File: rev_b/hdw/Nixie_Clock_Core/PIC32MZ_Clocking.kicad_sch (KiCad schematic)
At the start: 17 parts, among them U1101 74LVC1G97, X1101 ASE-8.000MHz, X1102 ECS-327KE

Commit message: lots of rev B control board schematic progress
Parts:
- renumbered C1103 to C?, C1105 to C?, C1101 to C?, C1104 to C?, C1102 to C?, L1102 to L?, L1101 to L?, R1101 to R?, R1105 to R?, R1103 to R?, R1102 to R?, R1104 to R?, R1106 to R?, TP1101 to TP?, U1101 to U?, X1101 to X?, X1102 to X?

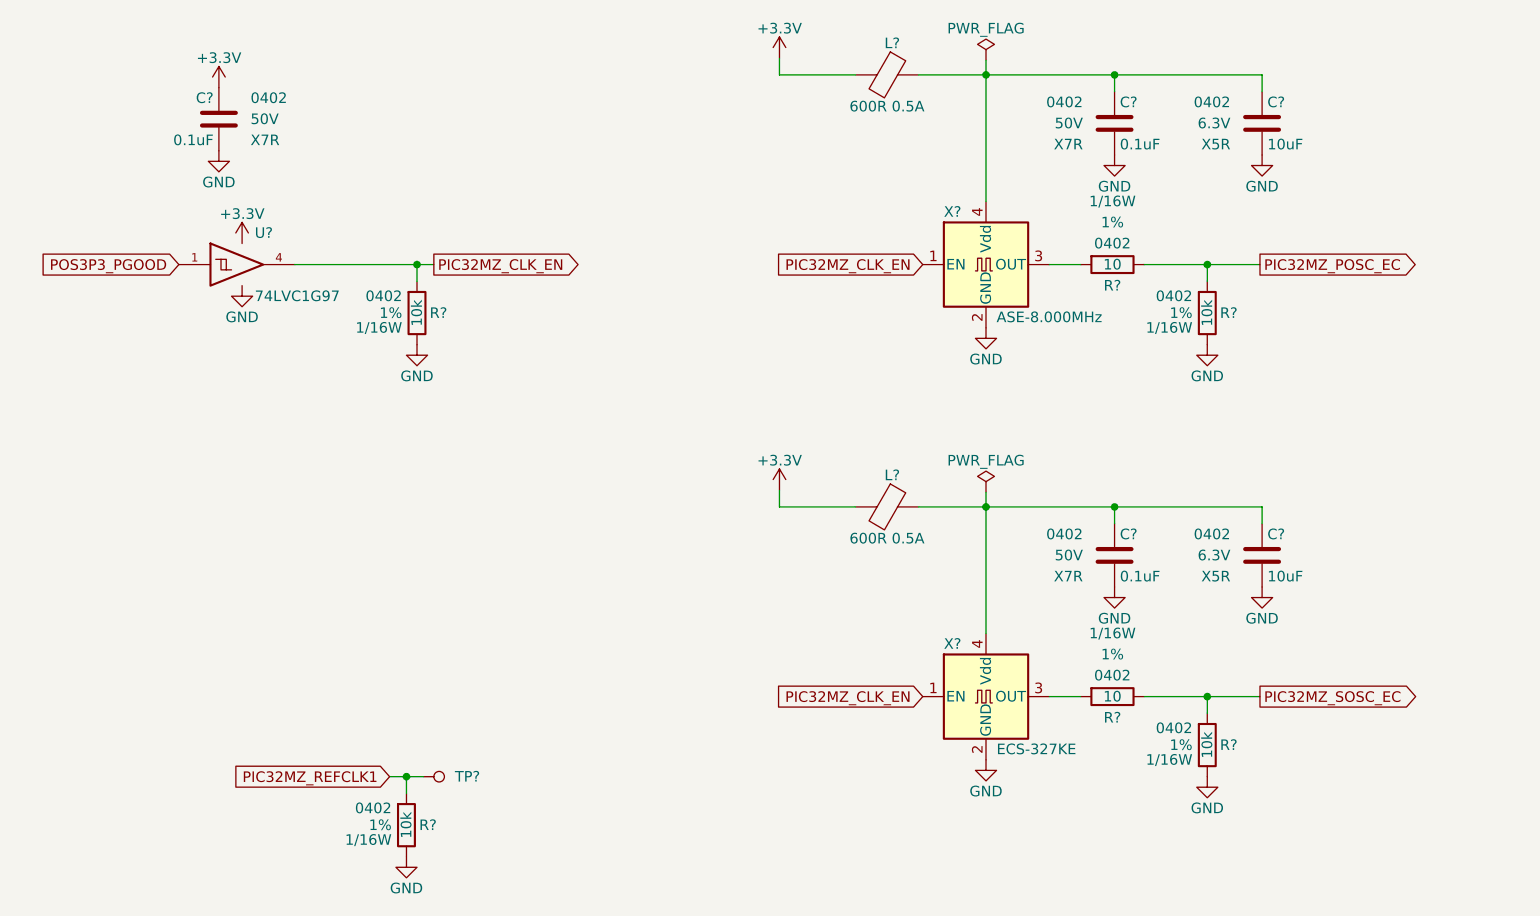
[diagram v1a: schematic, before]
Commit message: updated footprints, ran some DRC
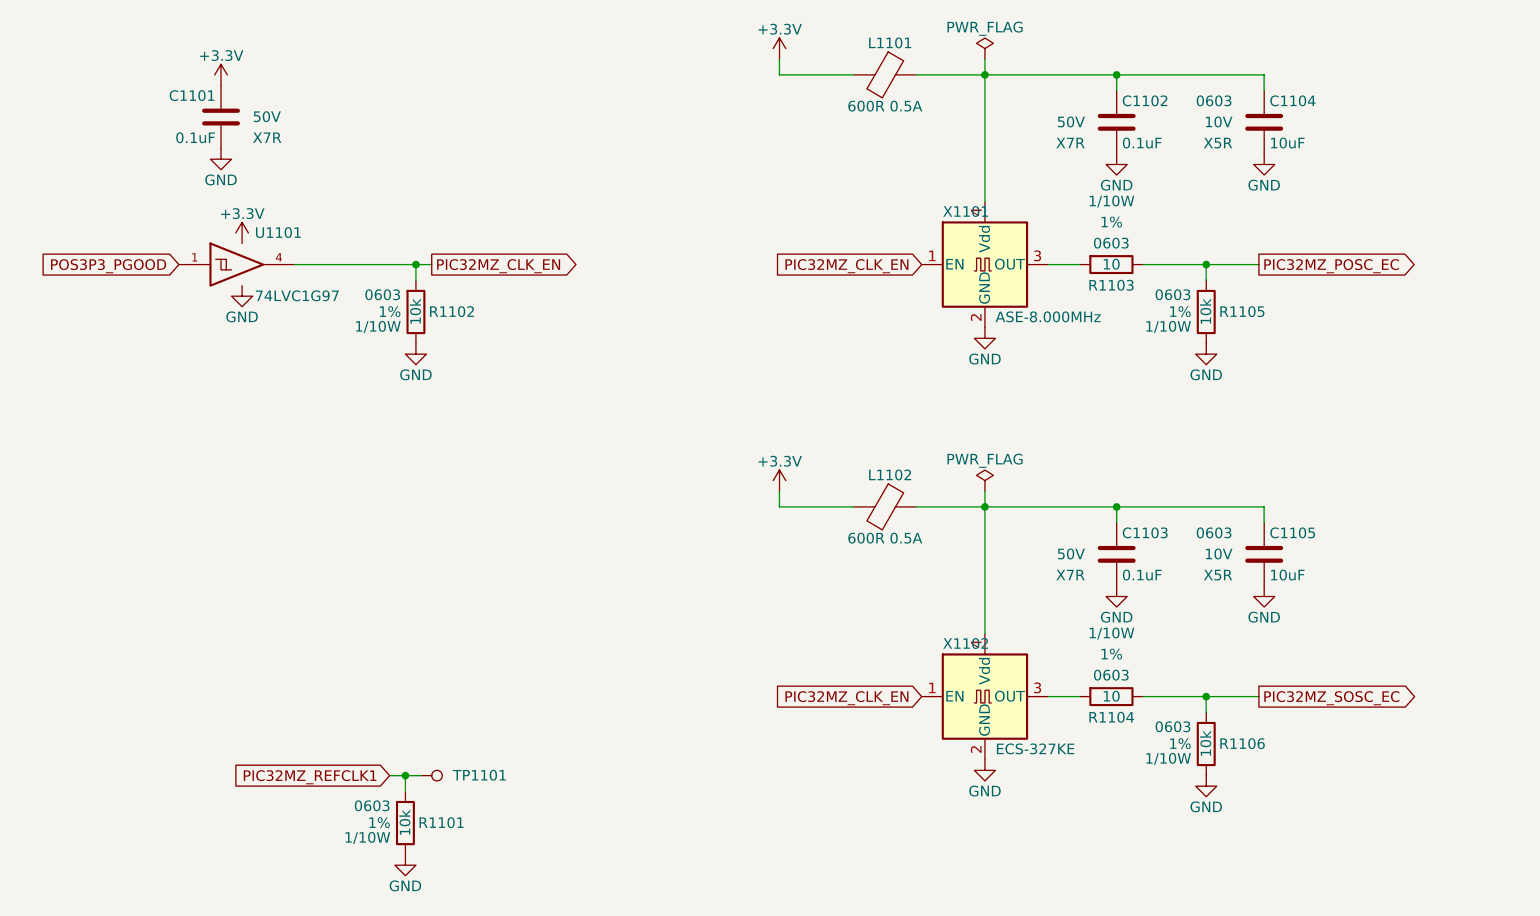
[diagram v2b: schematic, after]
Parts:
- C1101, C1102, C1103: renamed from C?; footprint Capacitors_SMD:C_0402 -> Capacitors_SMD:C_0603; Digi-Key PN 490-10698-1-ND -> (none); display_footprint 0402 -> (none)
- C1104, C1105: renamed from C?; footprint Capacitors_SMD:C_0402 -> Capacitors_SMD:C_0603; Digi-Key PN 1276-1451-1-ND -> (none); Voltage 6.3V -> 10V; display_footprint 0402 -> 0603
- L1101, L1102: renamed from L?; footprint Inductors_SMD:L_0402 -> Inductors_SMD:L_0603; Digi-Key PN 490-5441-1-ND -> (none)
- R1101, R1102, R1105, R1106: renamed from R?; footprint Resistors_SMD:R_0402 -> Resistors_SMD:R_0603; Digi-Key PN RMCF0402FT10K0CT-ND -> (none); Wattage 1/16W -> 1/10W; display_footprint 0402 -> 0603
- R1103, R1104: renamed from R?; footprint Resistors_SMD:R_0402 -> Resistors_SMD:R_0603; Digi-Key PN RMCF0402FT10R0CT-ND -> (none); Wattage 1/16W -> 1/10W; display_footprint 0402 -> 0603
- gave numbers to parts that had none: 4

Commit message: hid all passive refdes on core PCB
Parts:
- C1101, C1102, C1103: Digi-Key PN (none) -> 1276-1935-1-ND; display_footprint (none) -> 0603
- C1104, C1105: Digi-Key PN (none) -> 1276-1871-1-ND
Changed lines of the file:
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@@
       (effects (font (size 1.27 1.27)) hide)
     )
-    (property "display_footprint" "" (at 167.64 100.965 0)
+    (property "display_footprint" "0603" (at 167.64 100.965 0)
       (effects (font (size 1.27 1.27)) (justify right))
     )
@@
       (effects (font (size 1.27 1.27)) (justify right))
     )
-    (property "Digi-Key PN" "" (at 72.136 278.257 0)
+    (property "Digi-Key PN" "1276-1935-1-ND" (at 72.136 278.257 0)
       (effects (font (size 1.27 1.27)) hide)
     )
@@
       (effects (font (size 1.27 1.27)) (justify right))
     )
-    (property "Digi-Key PN" "" (at 189.23 103.505 0)
+    (property "Digi-Key PN" "1276-1871-1-ND" (at 189.23 103.505 0)
       (effects (font (size 1.27 1.27)) hide)
     )
@@
       (effects (font (size 1.27 1.27)) hide)
     )
-    (property "Digi-Key PN" "" (at 52.705 38.1 0)
+    (property "Digi-Key PN" "1276-1935-1-ND" (at 52.705 38.1 0)
       (effects (font (size 1.524 1.524)) hide)
     )
-    (property "display_footprint" "" (at 67.31 48.26 0)
+    (property "display_footprint" "0603" (at 67.31 48.26 0)
       (effects (font (size 1.27 1.27)) (justify right))
     )
@@
       (effects (font (size 1.27 1.27)) (justify right))
     )
-    (property "Digi-Key PN" "" (at 189.23 51.435 0)
+    (property "Digi-Key PN" "1276-1871-1-ND" (at 189.23 51.435 0)
       (effects (font (size 1.27 1.27)) hide)
     )
@@
       (effects (font (size 1.27 1.27)) hide)
     )
-    (property "display_footprint" "" (at 167.64 48.895 0)
+    (property "display_footprint" "0603" (at 167.64 48.895 0)
       (effects (font (size 1.27 1.27)) (justify right))
     )
@@
       (effects (font (size 1.27 1.27)) (justify right))
     )
-    (property "Digi-Key PN" "" (at 72.136 226.187 0)
-      (effects (font (size 1.27 1.27)) hide)
-    )
+    (property "Digi-Key PN" "1276-1935-1-ND" (at 72.136 226.187 0)
+      (effects (font (size 1.27 1.27)) hide)
+    )

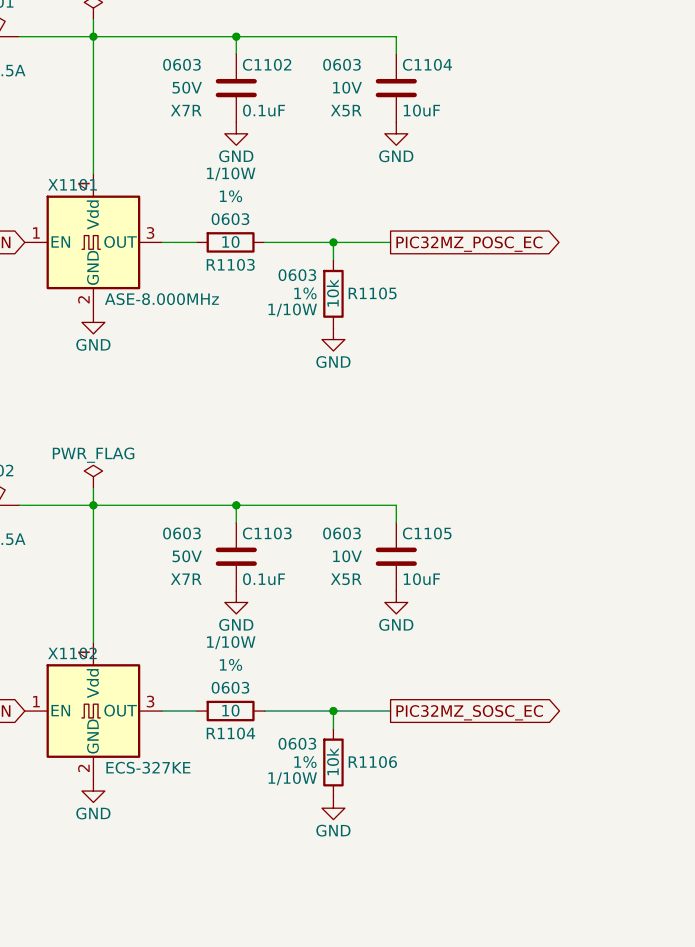
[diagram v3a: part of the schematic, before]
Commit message: started grouping MCU components on PCB
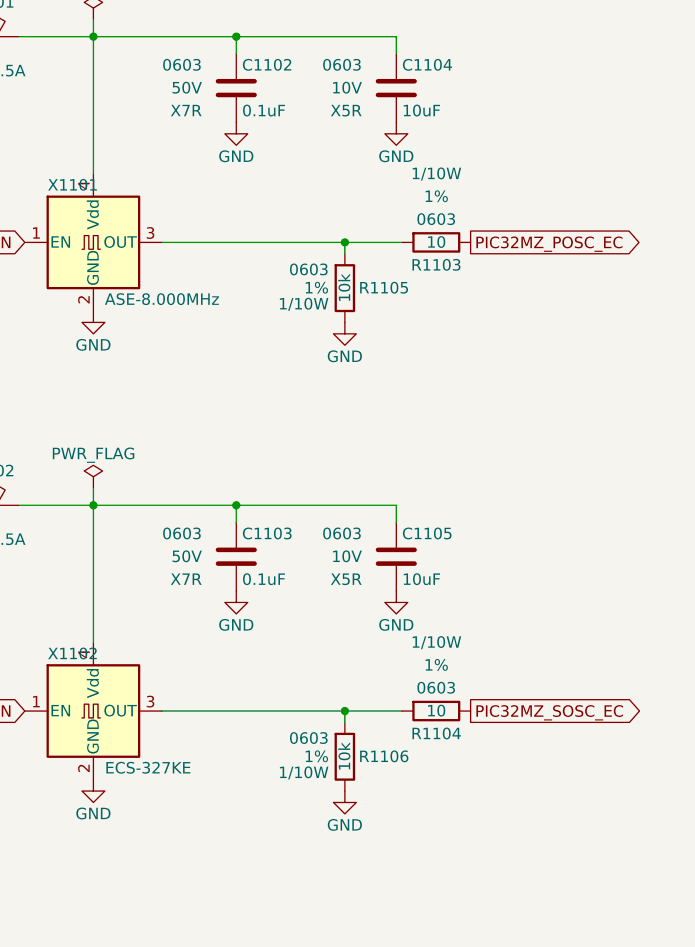
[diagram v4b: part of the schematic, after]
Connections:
- net PIC32MZ_POSC_EC: no longer R1105.1
- net PIC32MZ_SOSC_EC: no longer R1106.1
- net at R1103.1, X1101.3 (OUT): now also R1105.1
- net at R1104.1, X1102.3 (OUT): now also R1106.1
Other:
- moved on the sheet: R1103, R1104, R1105, R1106

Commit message: added BOM
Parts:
- L1101, L1102: Digi-Key PN (none) -> 490-1014-1-ND
- R1101, R1102, R1105, R1106: Digi-Key PN (none) -> 541-10.0KHCT-ND
- R1103, R1104: Digi-Key PN (none) -> 541-10.0HCT-ND
- U1101: Digi-Key PN 1727-1772-1-ND -> 296-15582-1-ND
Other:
- title: (none) -> Nixie Clock Redux Core Board
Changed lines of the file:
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@@
   (paper "A")
   (title_block
-    (date "2023-05-12")
-    (rev "PRELIM")
+    (title "Nixie Clock Redux Core Board")
+    (date "2023-07-30")
+    (rev "B")
     (company "Drew Maatman")
   )
@@
     (stroke (width 0) (type default))
   )
-  (global_label "PIC32MZ_CLK_EN" (shape input) (at 147.955 68.58 180)
+  (global_label "PIC32MZ_CLK_EN" (shape input) (at 147.955 68.58 180) (fields_autoplaced)
     (effects (font (size 1.27 1.27)) (justify right))
-    (property "Intersheetrefs" "${INTERSHEET_REFS}" (at 147.955 68.58 0)
-      (effects (font (size 1.27 1.27)) hide)
-    )
-  )
-  (global_label "PIC32MZ_REFCLK1" (shape input) (at 83.82 130.175 180)
+    (property "Intersheetrefs" "${INTERSHEET_REFS}" (at 128.8417 68.58 0)
+      (effects (font (size 1.27 1.27)) (justify right))
+    )
+  )
+  (global_label "PIC32MZ_REFCLK1" (shape input) (at 83.82 130.175 180) (fields_autoplaced)
     (effects (font (size 1.27 1.27)) (justify right))
-    (property "Intersheetrefs" "${INTERSHEET_REFS}" (at 83.82 130.175 0)
-      (effects (font (size 1.27 1.27)) hide)
-    )
-  )
-  (global_label "POS3P3_PGOOD" (shape input) (at 58.42 68.58 180)
+    (property "Intersheetrefs" "${INTERSHEET_REFS}" (at 63.4367 130.175 0)
+      (effects (font (size 1.27 1.27)) (justify right))
+    )
+  )
+  (global_label "POS3P3_PGOOD" (shape input) (at 58.42 68.58 180) (fields_autoplaced)
     (effects (font (size 1.27 1.27)) (justify right))
-    (property "Intersheetrefs" "${INTERSHEET_REFS}" (at 58.42 68.58 0)
-      (effects (font (size 1.27 1.27)) hide)
-    )
-  )
-  (global_label "PIC32MZ_SOSC_EC" (shape output) (at 197.485 120.65 0)
+    (property "Intersheetrefs" "${INTERSHEET_REFS}" (at 40.5766 68.58 0)
+      (effects (font (size 1.27 1.27)) (justify right))
+    )
+  )
+  (global_label "PIC32MZ_SOSC_EC" (shape output) (at 197.485 120.65 0) (fields_autoplaced)
     (effects (font (size 1.27 1.27)) (justify left))
-    (property "Intersheetrefs" "${INTERSHEET_REFS}" (at 197.485 120.65 0)
-      (effects (font (size 1.27 1.27)) hide)
-    )
-  )
-  (global_label "PIC32MZ_POSC_EC" (shape output) (at 197.485 68.58 0)
+    (property "Intersheetrefs" "${INTERSHEET_REFS}" (at 217.9892 120.65 0)
+      (effects (font (size 1.27 1.27)) (justify left))
+    )
+  )
+  (global_label "PIC32MZ_POSC_EC" (shape output) (at 197.485 68.58 0) (fields_autoplaced)
     (effects (font (size 1.27 1.27)) (justify left))
-    (property "Intersheetrefs" "${INTERSHEET_REFS}" (at 197.485 68.58 0)
-      (effects (font (size 1.27 1.27)) hide)
-    )
-  )
-  (global_label "PIC32MZ_CLK_EN" (shape output) (at 88.9 68.58 0)
+    (property "Intersheetrefs" "${INTERSHEET_REFS}" (at 218.0497 68.58 0)
+      (effects (font (size 1.27 1.27)) (justify left))
+    )
+  )
+  (global_label "PIC32MZ_CLK_EN" (shape output) (at 88.9 68.58 0) (fields_autoplaced)
     (effects (font (size 1.27 1.27)) (justify left))
-    (property "Intersheetrefs" "${INTERSHEET_REFS}" (at 88.9 68.58 0)
-      (effects (font (size 1.27 1.27)) hide)
-    )
-  )
-  (global_label "PIC32MZ_CLK_EN" (shape input) (at 147.955 120.65 180)
+    (property "Intersheetrefs" "${INTERSHEET_REFS}" (at 108.0133 68.58 0)
+      (effects (font (size 1.27 1.27)) (justify left))
+    )
+  )
+  (global_label "PIC32MZ_CLK_EN" (shape input) (at 147.955 120.65 180) (fields_autoplaced)
     (effects (font (size 1.27 1.27)) (justify right))
-    (property "Intersheetrefs" "${INTERSHEET_REFS}" (at 147.955 120.65 0)
-      (effects (font (size 1.27 1.27)) hide)
+    (property "Intersheetrefs" "${INTERSHEET_REFS}" (at 128.8417 120.65 0)
+      (effects (font (size 1.27 1.27)) (justify right))
     )
   )
@@
       (effects (font (size 1.27 1.27)) hide)
     )
-    (property "Digi-Key PN" "1727-1772-1-ND" (at 66.04 68.58 0)
+    (property "Digi-Key PN" "296-15582-1-ND" (at 66.04 68.58 0)
       (effects (font (size 1.27 1.27)) hide)
     )
@@
       (effects (font (size 1.27 1.27)) (justify left))
     )
-    (property "Digi-Key PN" "" (at 85.725 135.89 0)
+    (property "Digi-Key PN" "541-10.0KHCT-ND" (at 85.725 135.89 0)
       (effects (font (size 1.27 1.27)) hide)
     )
@@
       (effects (font (size 1.27 1.27)) hide)
     )
-    (property "Digi-Key PN" "" (at 65.024 -110.236 0)
+    (property "Digi-Key PN" "490-1014-1-ND" (at 65.024 -110.236 0)
       (effects (font (size 1.27 1.27)) hide)
     )
@@
       (effects (font (size 1.27 1.27)) hide)
     )
-    (property "Digi-Key PN" "" (at 65.024 -162.306 0)
+    (property "Digi-Key PN" "490-1014-1-ND" (at 65.024 -162.306 0)
       (effects (font (size 1.27 1.27)) hide)
     )
@@
       (effects (font (size 1.27 1.27)) (justify left))
     )
-    (property "Digi-Key PN" "" (at 183.515 73.66 0)
+    (property "Digi-Key PN" "541-10.0KHCT-ND" (at 183.515 73.66 0)
       (effects (font (size 1.27 1.27)) hide)
     )
@@
       (effects (font (size 1.27 1.27)))
     )
-    (property "Digi-Key PN" "" (at 183.515 60.96 0)
+    (property "Digi-Key PN" "541-10.0HCT-ND" (at 183.515 60.96 0)
       (effects (font (size 1.524 1.524)) hide)
     )
@@
       (effects (font (size 1.27 1.27)) (justify left))
     )
-    (property "Digi-Key PN" "" (at 86.995 74.295 0)
+    (property "Digi-Key PN" "541-10.0KHCT-ND" (at 86.995 74.295 0)
       (effects (font (size 1.27 1.27)) hide)
     )
@@
       (effects (font (size 1.27 1.27)))
     )
-    (property "Digi-Key PN" "" (at 183.515 113.03 0)
+    (property "Digi-Key PN" "541-10.0HCT-ND" (at 183.515 113.03 0)
       (effects (font (size 1.524 1.524)) hide)
     )
@@
       (effects (font (size 1.27 1.27)) (justify left))
     )
-    (property "Digi-Key PN" "" (at 183.515 125.73 0)
-      (effects (font (size 1.27 1.27)) hide)
-    )
+    (property "Digi-Key PN" "541-10.0KHCT-ND" (at 183.515 125.73 0)
+      (effects (font (size 1.27 1.27)) hide)
+    )
